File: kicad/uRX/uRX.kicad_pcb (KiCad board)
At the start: 2 copper layers, 166 parts, among them J1 RF_AM_GND, J10 GPIO_A, J11 Bat1, J2 C165948, J3 Loudspeaker, J4 Display, J6 U.FL, J8 Bat0, J9 RF_AM__In, Q1 BC847, SW1 RotaryEncoder_Switch, SW2 SW_DPDT_x2, SW3 Reset, SW4 Boot, U1 CBT3253, U10 IP2326, U11 LP2985-5.0, U12 OPA2211, U13 HT733333, U2 LM4562, U3 PAM8406D, U4 Si5351A-B-GT, U5 ESP32-S3-WROOM-2, U6 Si4732-A10, U7 PCM1808PWR, U8 LM4040-2.5, U9 PCM1808PWR, X1 X322525MOB4SI, Y2 32768kHz

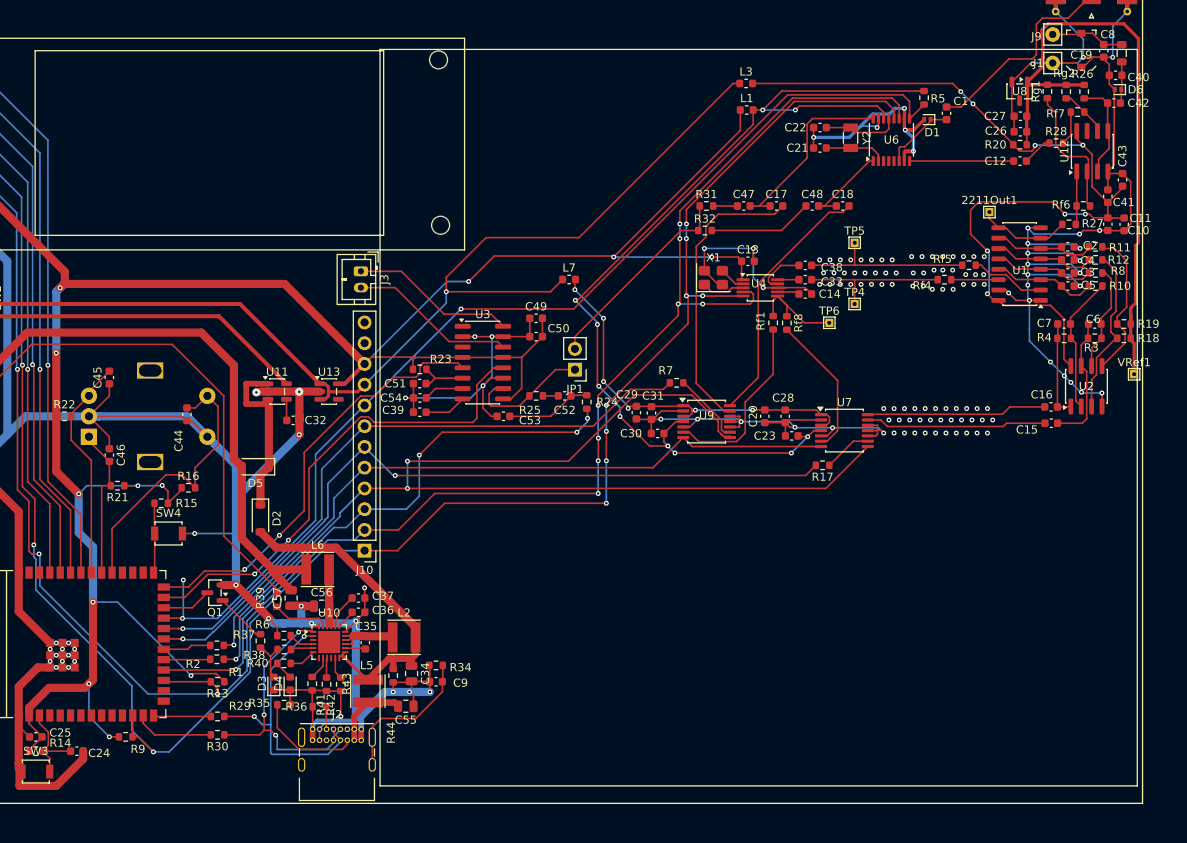
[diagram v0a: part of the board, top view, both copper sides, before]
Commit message: add e-inc wiring
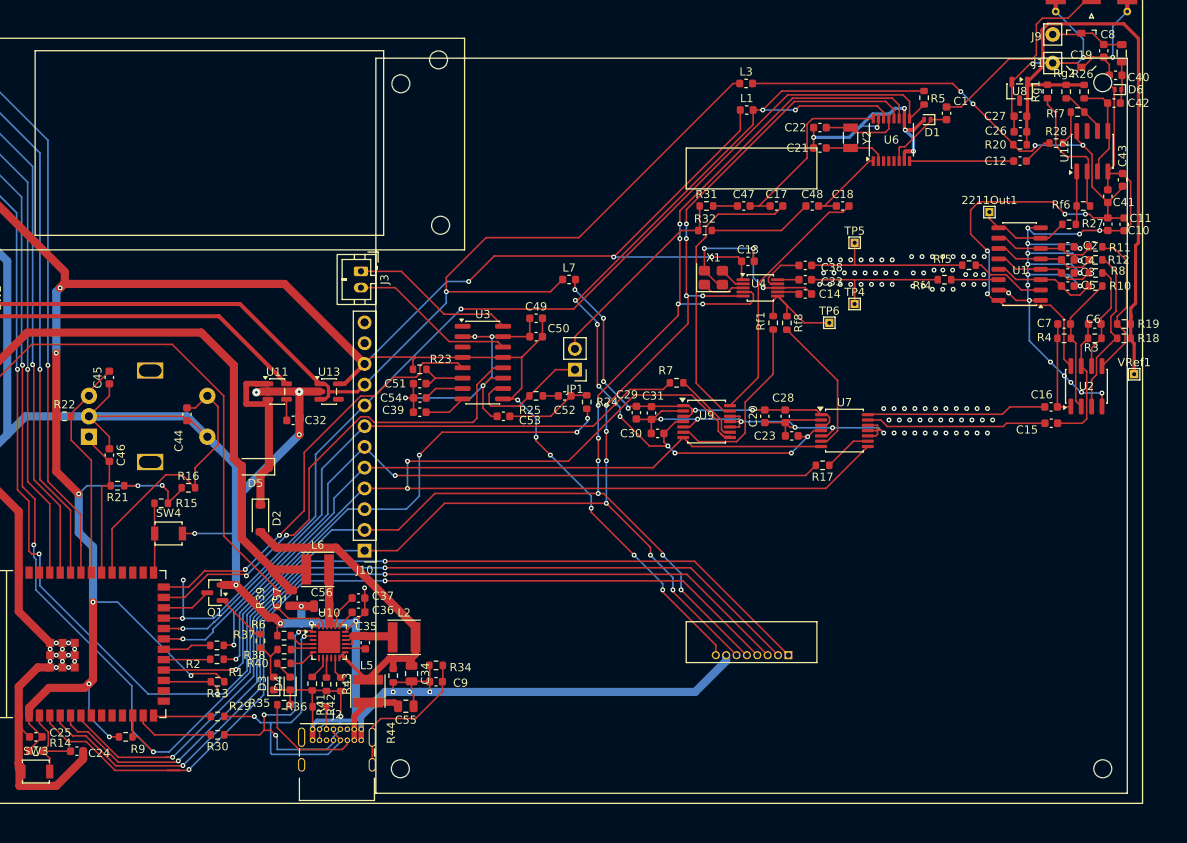
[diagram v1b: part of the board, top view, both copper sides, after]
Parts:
- added J5: e-ink, Connector_PinHeader_1.27mm:PinHeader_1x08_P1.27mm_Horizontal, B.Cu at (181.9, 121.0)
- added M2: , MountingHole:MountingHole_2.2mm_M2_DIN965, F.Cu at (134.4, 134.9)
- added M2: , MountingHole:MountingHole_2.2mm_M2_DIN965, F.Cu at (134.4, 51.0)
- added M2: , MountingHole:MountingHole_2.2mm_M2_DIN965, F.Cu at (220.4, 134.9)
- added M2: , MountingHole:MountingHole_2.2mm_M2_DIN965, F.Cu at (220.4, 50.9)
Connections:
- U5 pad 4: unconnected-(U5-GPIO4/TOUCH4/ADC1_CH3-Pad4) -> /eInk_CS
- U5 pad 5: unconnected-(U5-GPIO5/TOUCH5/ADC1_CH4-Pad5) -> /eInk_DC
- U5 pad 6: unconnected-(U5-GPIO6/TOUCH6/ADC1_CH5-Pad6) -> /eInk_RES
- U5 pad 7: unconnected-(U5-GPIO7/TOUCH7/ADC1_CH6-Pad7) -> /eInk_BUSY
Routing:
- net /eInk_CS: track 0.00 -> 110.0 mm, vias 0 -> 2
- net /eInk_RES: track 0.00 -> 108.5 mm, vias 0 -> 2
- net /eInk_DC: track 0.00 -> 108.4 mm, vias 0 -> 2
- net /eInk_BUSY: track 0.00 -> 108.2 mm, vias 0 -> 2
- net +3.3V: track 288.8 -> 332.0 mm, vias 12 -> 18
- net GND: track 581.5 -> 619.8 mm
- net /SCL: track 234.0 -> 262.2 mm, vias 11 -> 13
- net /SDA: track 239.1 -> 264.8 mm, vias 11 -> 13
- net USB_D-: track 33.1 -> 35.0 mm
- net USB_D+: track 34.1 -> 35.4 mm

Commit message: feels like the schematics/pcb is complete
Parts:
- added R33: 4.7K, Resistor_SMD:R_0603_1608Metric, F.Cu at (179.8, 125.2)
- added R45: 4.7K, Resistor_SMD:R_0603_1608Metric, F.Cu at (176.7, 123.5)
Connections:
- C10 pad 2: GND -> +5VfilteredM
- C11 pad 2: GND -> +5VfilteredM
- C13 pad 2: GND -> +5VfilteredM
- C14 pad 2: GND -> +5VfilteredM
- C19 pad 1: GND -> +5VfilteredM
- C2 pad 2: GND -> +5VfilteredM
- C20 pad 1: GND -> +5VfilteredM
- C21 pad 1: GND -> +5VfilteredM
- C22 pad 1: GND -> +5VfilteredM
- C23 pad 1: GND -> +5VfilteredM
- C24 pad 2: GND -> +5VfilteredM
- C25 pad 2: GND -> +5VfilteredM
- C26 pad 2: GND -> +5VfilteredM
- C27 pad 2: GND -> +5VfilteredM
- C28 pad 1: GND -> +5VfilteredM
- C29 pad 1: GND -> +5VfilteredM
- C3 pad 2: GND -> +5VfilteredM
- C30 pad 1: GND -> +5VfilteredM
- C31 pad 1: GND -> +5VfilteredM
- C32 pad 2: GND -> +5VfilteredM
- C34 pad 2: GND -> +5VfilteredM
- C36 pad 2: GND -> +5VfilteredM
- C37 pad 2: GND -> +5VfilteredM
- C39 pad 1: GND -> +5VfilteredM
- C4 pad 2: GND -> +5VfilteredM
- C40 pad 2: GND -> +5VfilteredM
- C41 pad 2: GND -> +5VfilteredM
- C43 pad 2: GND -> +5VfilteredM
- C44 pad 2: GND -> +5VfilteredM
- C45 pad 1: GND -> +5VfilteredM
- C46 pad 1: GND -> +5VfilteredM
- C49 pad 1: GND -> +5VfilteredM
- C5 pad 2: GND -> +5VfilteredM
- C50 pad 1: GND -> +5VfilteredM
- C51 pad 1: GND -> +5VfilteredM
- C53 pad 1: GND -> +5VfilteredM
- C54 pad 1: GND -> +5VfilteredM
- C55 pad 1: GND -> +5VfilteredM
- C56 pad 1: GND -> +5VfilteredM
- C57 pad 1: GND -> +5VfilteredM
- C8 pad 2: GND -> +5VfilteredM
- C9 pad 2: GND -> +5VfilteredM
- D3 pad 1: GND -> +5VfilteredM
- D4 pad 1: GND -> +5VfilteredM
- D6 pad 2: GND -> +5VfilteredM
- J1 pad 1: GND -> +5VfilteredM
- J11 pad 1: GND -> +5VfilteredM
- J2 pad A1: GND -> +5VfilteredM
- J2 pad A12: GND -> +5VfilteredM
- J2 pad B1: GND -> +5VfilteredM
- J2 pad B12: GND -> +5VfilteredM
- J4 pad 1: GND -> +5VfilteredM
- J5 pad 7: GND -> +5VfilteredM
- J6 pad 2: GND -> +5VfilteredM
- NT1 pad 2: GND -> +5VfilteredM
- NT2 pad 2: GND -> +5VfilteredM
- Q1 pad 2: GND -> +5VfilteredM
- R34 pad 2: GND -> +5VfilteredM
- R35 pad 2: GND -> +5VfilteredM
- R36 pad 2: GND -> +5VfilteredM
- R37 pad 2: GND -> +5VfilteredM
- R41 pad 2: GND -> +5VfilteredM
- R42 pad 2: GND -> +5VfilteredM
- R43 pad 2: GND -> +5VfilteredM
- R44 pad 2: GND -> +5VfilteredM
- SW1 pad C: GND -> +5VfilteredM
- SW1 pad S2: GND -> +5VfilteredM
- SW3 pad 1: GND -> +5VfilteredM
- SW4 pad 2: GND -> +5VfilteredM
- U1 pad 1: GND -> +5VfilteredM
- U1 pad 15: GND -> +5VfilteredM
- U1 pad 8: GND -> +5VfilteredM
- U10 pad 18: GND -> +5VfilteredM
- U10 pad 24: GND -> +5VfilteredM
- U11 pad 2: GND -> +5VfilteredM
- U12 pad 4: GND -> +5VfilteredM
- U13 pad 2: GND -> +5VfilteredM
- U2 pad 4: GND -> +5VfilteredM
- U3 pad 11: GND -> +5VfilteredM
- U3 pad 15: GND -> +5VfilteredM
- U3 pad 2: GND -> +5VfilteredM
- U4 pad 8: GND -> +5VfilteredM
- U5 pad 1: GND -> +5VfilteredM
- U5 pad 40: GND -> +5VfilteredM
- U5 pad 41: GND -> +5VfilteredM
- U6 pad 10: GND -> +5VfilteredM
- U6 pad 15: GND -> +5VfilteredM
- U7 pad 10: GND -> +5VfilteredM
- U7 pad 11: GND -> +5VfilteredM
- U7 pad 12: GND -> +5VfilteredM
- U7 pad 2: GND -> +5VfilteredM
- U7 pad 5: GND -> +5VfilteredM
- U8 pad 2: GND -> +5VfilteredM
- U9 pad 10: GND -> +5VfilteredM
- U9 pad 11: GND -> +5VfilteredM
- U9 pad 12: GND -> +5VfilteredM
- U9 pad 2: GND -> +5VfilteredM
- U9 pad 5: GND -> +5VfilteredM
- X1 pad 2: GND -> +5VfilteredM
- X1 pad 4: GND -> +5VfilteredM
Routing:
- net +5VfilteredM: track 47.5 -> 667.3 mm, vias 6 -> 152
- net GND: track 619.8 -> 0.00 mm, vias 146 -> 0
- net +3.3V: track 332.0 -> 339.7 mm
- net /eInk_RES: track 108.5 -> 112.7 mm
- net /eInk_CS: track 110.0 -> 112.7 mm
- net /eInk_BUSY: track 108.2 -> 107.7 mm

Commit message: feels like the schematics/pcb is complete
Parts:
- removed the M2 at (220.4, 50.9)
- added L8: 180nH, PCM_JLCPCB:L_0805, F.Cu at (201.9, 57.2)
- added Q2: BC847, Package_TO_SOT_SMD:SOT-23, F.Cu at (87.5, 49.5)
- added R46: 2.2k, Resistor_SMD:R_0603_1608Metric, F.Cu at (91.5, 87.8)
- C1: value 100p -> 18p
- moved R22 5.53 mm to (95.0, 86.5)
- moved M2 1.10 mm to (135.0, 134.0)
- moved M2 1.10 mm to (221.0, 134.0)
- moved M2 1.10 mm to (135.1, 50.1)
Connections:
- C10 pad 2: +5VfilteredM -> GND
- C11 pad 2: +5VfilteredM -> GND
- C13 pad 2: +5VfilteredM -> GND
- C14 pad 2: +5VfilteredM -> GND
- C19 pad 1: +5VfilteredM -> GND
- C2 pad 2: +5VfilteredM -> GND
- C20 pad 1: +5VfilteredM -> GND
- C21 pad 1: +5VfilteredM -> GND
- C22 pad 1: +5VfilteredM -> GND
- C23 pad 1: +5VfilteredM -> GND
- C24 pad 2: +5VfilteredM -> GND
- C25 pad 2: +5VfilteredM -> GND
- C26 pad 2: +5VfilteredM -> GND
- C27 pad 2: +5VfilteredM -> GND
- C28 pad 1: +5VfilteredM -> GND
- C29 pad 1: +5VfilteredM -> GND
- C3 pad 2: +5VfilteredM -> GND
- C30 pad 1: +5VfilteredM -> GND
- C31 pad 1: +5VfilteredM -> GND
- C32 pad 2: +5VfilteredM -> GND
- C34 pad 2: +5VfilteredM -> GND
- C36 pad 2: +5VfilteredM -> GND
- C37 pad 2: +5VfilteredM -> GND
- C39 pad 1: +5VfilteredM -> GND
- C4 pad 2: +5VfilteredM -> GND
- C40 pad 2: +5VfilteredM -> GND
- C41 pad 2: +5VfilteredM -> GND
- C43 pad 2: +5VfilteredM -> GND
- C44 pad 2: +5VfilteredM -> GND
- C45 pad 1: +5VfilteredM -> GND
- C46 pad 1: +5VfilteredM -> GND
- C49 pad 1: +5VfilteredM -> GND
- C5 pad 2: +5VfilteredM -> GND
- C50 pad 1: +5VfilteredM -> GND
- C51 pad 1: +5VfilteredM -> GND
- C53 pad 1: +5VfilteredM -> GND
- C54 pad 1: +5VfilteredM -> GND
- C55 pad 1: +5VfilteredM -> GND
- C56 pad 1: +5VfilteredM -> GND
- C57 pad 1: +5VfilteredM -> GND
- C8 pad 2: +5VfilteredM -> GND
- C9 pad 2: +5VfilteredM -> GND
- D3 pad 1: +5VfilteredM -> GND
- D4 pad 1: +5VfilteredM -> GND
- D6 pad 2: +5VfilteredM -> GND
- J1 pad 1: +5VfilteredM -> GND
- J11 pad 1: +5VfilteredM -> GND
- J2 pad A1: +5VfilteredM -> GND
- J2 pad A12: +5VfilteredM -> GND
- J2 pad B1: +5VfilteredM -> GND
- J2 pad B12: +5VfilteredM -> GND
- J4 pad 1: +5VfilteredM -> GND
- J5 pad 7: +5VfilteredM -> GND
- J6 pad 2: +5VfilteredM -> GND
- NT1 pad 2: +5VfilteredM -> GND
- NT2 pad 2: +5VfilteredM -> GND
- Q1 pad 2: +5VfilteredM -> GND
- R34 pad 2: +5VfilteredM -> GND
- R35 pad 2: +5VfilteredM -> GND
- R36 pad 2: +5VfilteredM -> GND
- R37 pad 2: +5VfilteredM -> GND
- R41 pad 2: +5VfilteredM -> GND
- R42 pad 2: +5VfilteredM -> GND
- R43 pad 2: +5VfilteredM -> GND
- R44 pad 2: +5VfilteredM -> GND
- SW1 pad C: +5VfilteredM -> GND
- SW1 pad S2: +5VfilteredM -> GND
- SW3 pad 1: +5VfilteredM -> GND
- SW4 pad 2: +5VfilteredM -> GND
- U1 pad 1: +5VfilteredM -> GND
- U1 pad 15: +5VfilteredM -> GND
- U1 pad 8: +5VfilteredM -> GND
- U10 pad 18: +5VfilteredM -> GND
- U10 pad 24: +5VfilteredM -> GND
- U11 pad 2: +5VfilteredM -> GND
- U12 pad 4: +5VfilteredM -> GND
- U13 pad 2: +5VfilteredM -> GND
- U2 pad 4: +5VfilteredM -> GND
- U3 pad 11: +5VfilteredM -> GND
- U3 pad 15: +5VfilteredM -> GND
- U3 pad 2: +5VfilteredM -> GND
- U4 pad 8: +5VfilteredM -> GND
- U5 pad 1: +5VfilteredM -> GND
- U5 pad 34: /D_BLK -> Net-(U5-MTDI/GPIO41/CLK_OUT1)
- U5 pad 40: +5VfilteredM -> GND
- U5 pad 41: +5VfilteredM -> GND
- U6 pad 10: +5VfilteredM -> GND
- U6 pad 15: +5VfilteredM -> GND
- U7 pad 10: +5VfilteredM -> GND
- U7 pad 11: +5VfilteredM -> GND
- U7 pad 12: +5VfilteredM -> GND
- U7 pad 2: +5VfilteredM -> GND
- U7 pad 5: +5VfilteredM -> GND
- U8 pad 2: +5VfilteredM -> GND
- U9 pad 10: +5VfilteredM -> GND
- U9 pad 11: +5VfilteredM -> GND
- U9 pad 12: +5VfilteredM -> GND
- U9 pad 2: +5VfilteredM -> GND
- U9 pad 5: +5VfilteredM -> GND
- X1 pad 2: +5VfilteredM -> GND
- X1 pad 4: +5VfilteredM -> GND
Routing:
- net GND: track 0.00 -> 703.8 mm, vias 0 -> 53
- net +5VfilteredM: track 667.3 -> 47.5 mm, vias 152 -> 18
- net /D_BLK: track 66.5 -> 3.77 mm, vias 1 -> 0
- net Net-(Q2-B): track 0.00 -> 37.7 mm, vias 0 -> 2
- net Net-(U5-MTDI/GPIO41/CLK_OUT1): track 0.00 -> 23.9 mm
- net +3.3V: track 339.7 -> 335.0 mm
- net Net-(J6-In): track 25.6 -> 29.0 mm
- net Net-(U5-MTDO/GPIO40/CLK_OUT2): track 26.8 -> 29.8 mm
- net /AUDIO_SHND: track 60.0 -> 60.6 mm

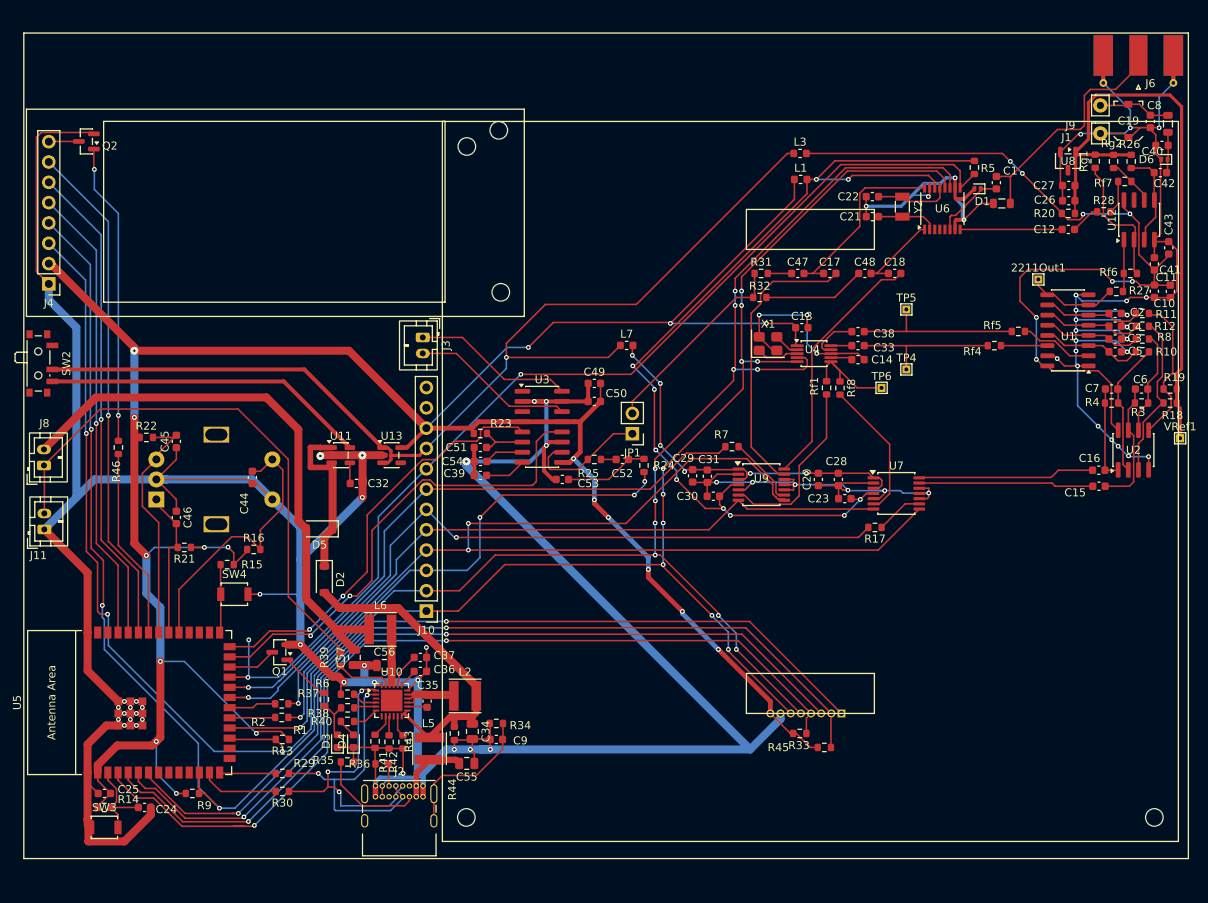
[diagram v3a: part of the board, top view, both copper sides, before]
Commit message: correct i2c - mosi/sclk
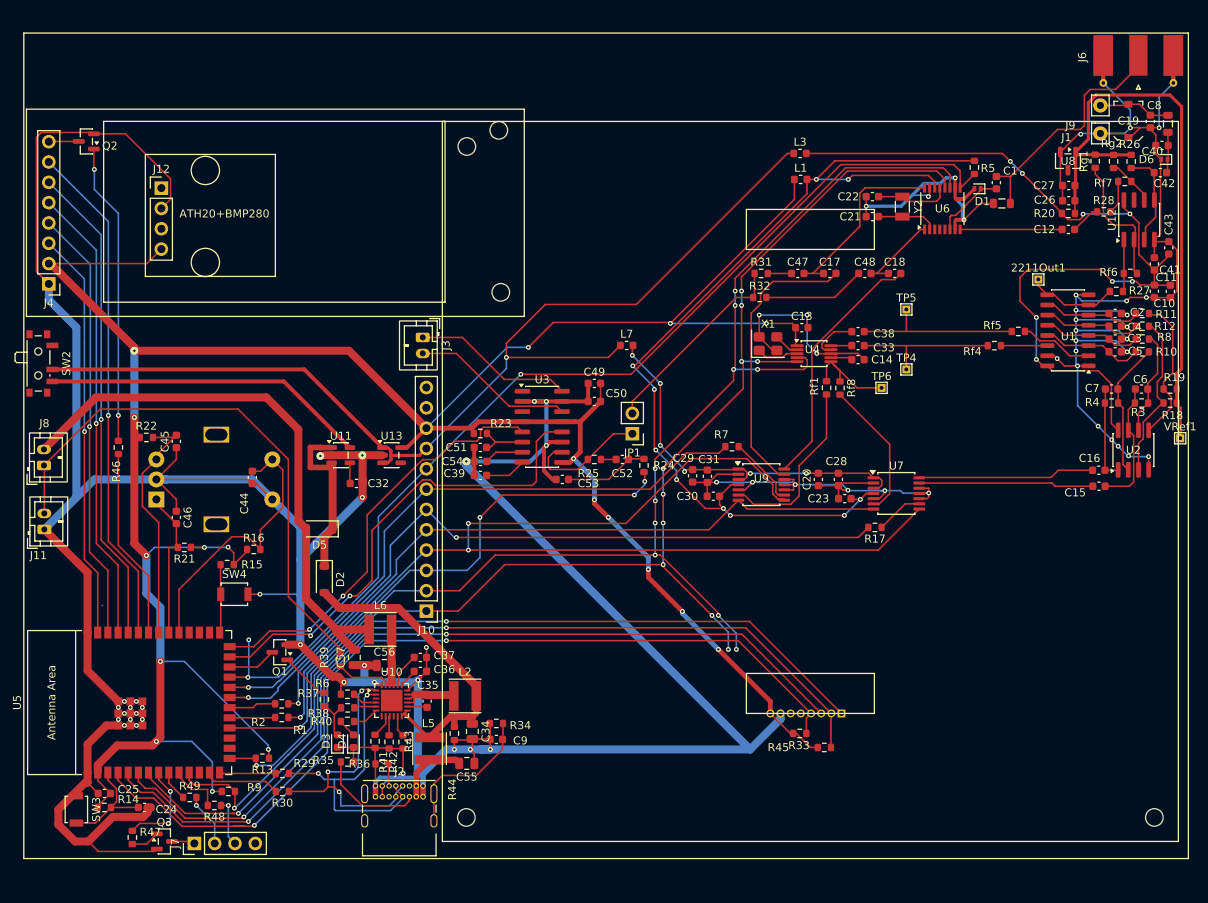
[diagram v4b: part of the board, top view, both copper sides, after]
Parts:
- added J12: TPH, Connector_PinHeader_2.54mm:PinHeader_1x04_P2.54mm_Vertical, F.Cu at (96.9, 55.3)
- added J7: GPS, Connector_PinHeader_2.54mm:PinHeader_1x04_P2.54mm_Vertical, F.Cu at (101.0, 137.2)
- added Q3: BC847, Package_TO_SOT_SMD:SOT-23, F.Cu at (97.2, 137.0)
- added R47: 1k, Resistor_SMD:R_0603_1608Metric, F.Cu at (93.2, 136.5)
- added R48: 100, Resistor_SMD:R_0603_1608Metric, F.Cu at (103.5, 132.5)
- added R49: 100, Resistor_SMD:R_0603_1608Metric, F.Cu at (100.4, 131.5)
- moved R9 4.51 mm to (105.2, 130.8)
- moved SW3 4.16 mm to (86.2, 133.0), turned to -90 degrees
- moved R13 3.43 mm to (109.5, 126.6)
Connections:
- net Net-(U7-VINL) renamed /I_CHANNEL
- net Net-(U7-VINR) renamed /Q_CHANNEL
- J4 pad 3: /SCL -> /SCLK
- J4 pad 4: /SDA -> /MOSI
- J5 pad 5: /SCL -> /SCLK
- J5 pad 6: /SDA -> /MOSI
- U5 pad 10: unconnected-(U5-GPIO17/U1TXD/ADC2_CH6-Pad10) -> Net-(U5-GPIO17/U1TXD/ADC2_CH6)
- U5 pad 11: unconnected-(U5-GPIO18/U1RXD/ADC2_CH7/CLK_OUT3-Pad11) -> /SDA
- U5 pad 12: /SDA -> unconnected-(U5-GPIO8/TOUCH8/ADC1_CH7/SUBSPICS1-Pad12)
- U5 pad 15: unconnected-(U5-GPIO3/TOUCH3/ADC1_CH2-Pad15) -> /SCL
- U5 pad 17: /SCL -> unconnected-(U5-GPIO9/TOUCH9/ADC1_CH8/FSPIHD/SUBSPIHD-Pad17)
- U5 pad 38: unconnected-(U5-GPIO2/TOUCH2/ADC1_CH1-Pad38) -> /MOSI
- U5 pad 39: unconnected-(U5-GPIO1/TOUCH1/ADC1_CH0-Pad39) -> /SCLK
- U5 pad 8: unconnected-(U5-GPIO15/U0RTS/ADC2_CH4/XTAL_32K_P-Pad8) -> Net-(U5-GPIO15/U0RTS/ADC2_CH4/XTAL_32K_P)
- U5 pad 9: unconnected-(U5-GPIO16/U0CTS/ADC2_CH5/XTAL_32K_N-Pad9) -> Net-(U5-GPIO16/U0CTS/ADC2_CH5/XTAL_32K_N)
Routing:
- net /SCL: track 262.1 -> 170.1 mm, vias 13 -> 11
- net /SDA: track 264.8 -> 173.3 mm, vias 13 -> 11
- net /MOSI: track 0.00 -> 54.3 mm, vias 0 -> 1
- net /SCLK: track 0.00 -> 51.2 mm, vias 0 -> 1
- net GND: track 703.8 -> 731.9 mm
- net +3.3V: track 335.0 -> 353.2 mm
- net Net-(U5-GPIO15/U0RTS/ADC2_CH4/XTAL_32K_P): track 0.00 -> 12.0 mm, vias 0 -> 2
- net Net-(U5-GPIO17/U1TXD/ADC2_CH6): track 0.00 -> 6.76 mm
- net /TX: track 0.00 -> 6.70 mm, vias 0 -> 1
- net /RX: track 0.00 -> 6.02 mm, vias 0 -> 1
- net Net-(U5-GPIO16/U0CTS/ADC2_CH5/XTAL_32K_N): track 0.00 -> 3.85 mm
- net Net-(Q3-B): track 0.00 -> 3.59 mm
- net /SW_GND: track 0.00 -> 2.92 mm
- net Net-(U5-EN): track 11.4 -> 13.7 mm
- net unconnected-(U5-GPIO8/TOUCH8/ADC1_CH7/SUBSPICS1-Pad12): track 0.00 -> 0.53 mm
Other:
- board text added: "ATH20+BMP280"

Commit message: cleanup
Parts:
- moved J12 73.3 mm to (147.3, 108.5), turned to -90 degrees
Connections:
- J12 pad 1: /SCL -> +3.3V
- J12 pad 2: GND -> /SDA
- J12 pad 3: /SDA -> GND
- J12 pad 4: +3.3V -> /SCL
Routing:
- net /SCLK: track 51.2 -> 174.6 mm, vias 1 -> 6
- net /MOSI: track 54.3 -> 175.7 mm, vias 1 -> 6
- net GND: track 731.9 -> 745.5 mm
- net /SCL: track 170.1 -> 164.7 mm, vias 11 -> 9
- net /eInk_CS: track 112.7 -> 110.5 mm
- net +3.3V: track 353.2 -> 350.9 mm
- net /eInk_DC: track 108.4 -> 106.4 mm
- net /SDA: track 173.3 -> 175.0 mm, vias 11 -> 9
- net /eInk_RES: track 112.7 -> 111.2 mm
- net /eInk_BUSY: track 107.7 -> 106.3 mm
